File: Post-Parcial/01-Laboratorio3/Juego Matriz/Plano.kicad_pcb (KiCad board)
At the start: 2 copper layers, 122.7 x 77 mm, 33 parts, among them J1 Conn_01x12, J2 Conn_01x12, J3 Conn_01x19, J4 Conn_01x19, Q1 2N3904, Q2 2N3904, Q3 2N3904, Q4 2N3904, Q5 2N3904, Q6 2N3904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

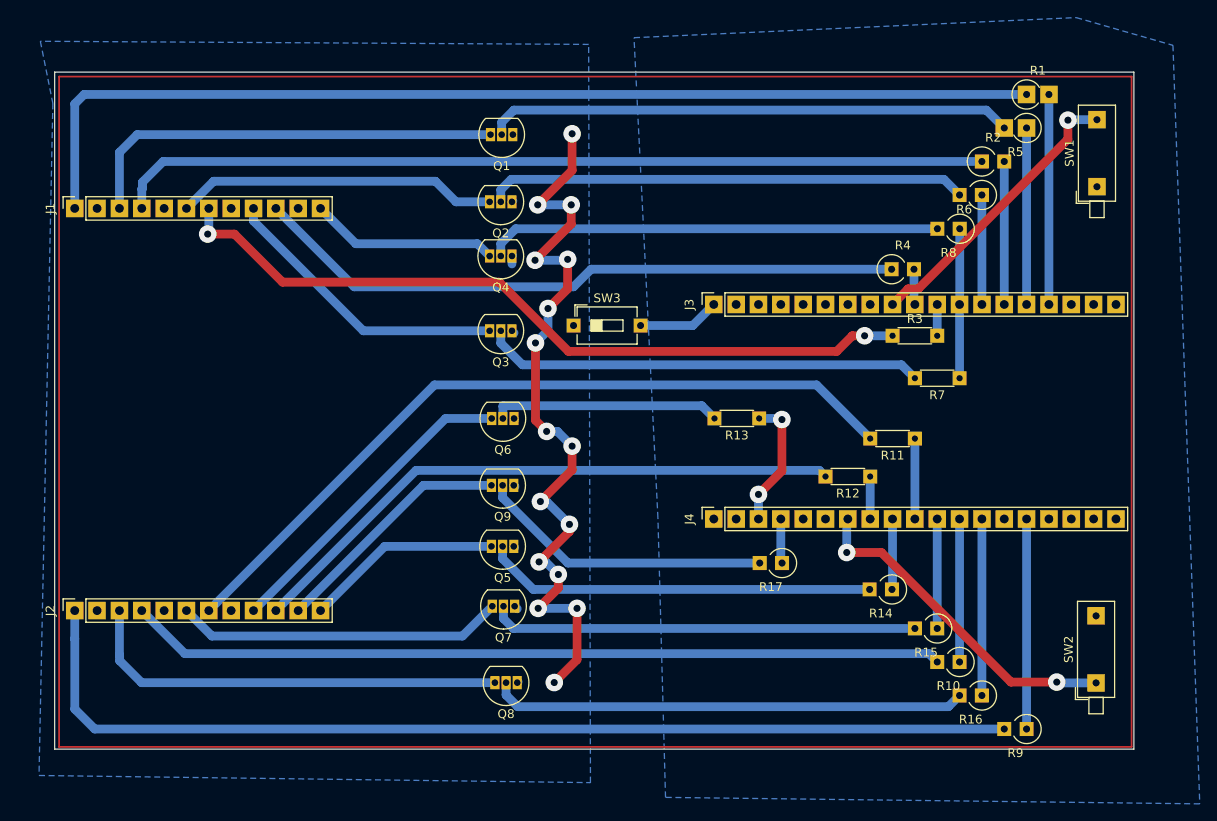
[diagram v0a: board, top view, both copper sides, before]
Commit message: Reorganización de PCB Juego Matriz
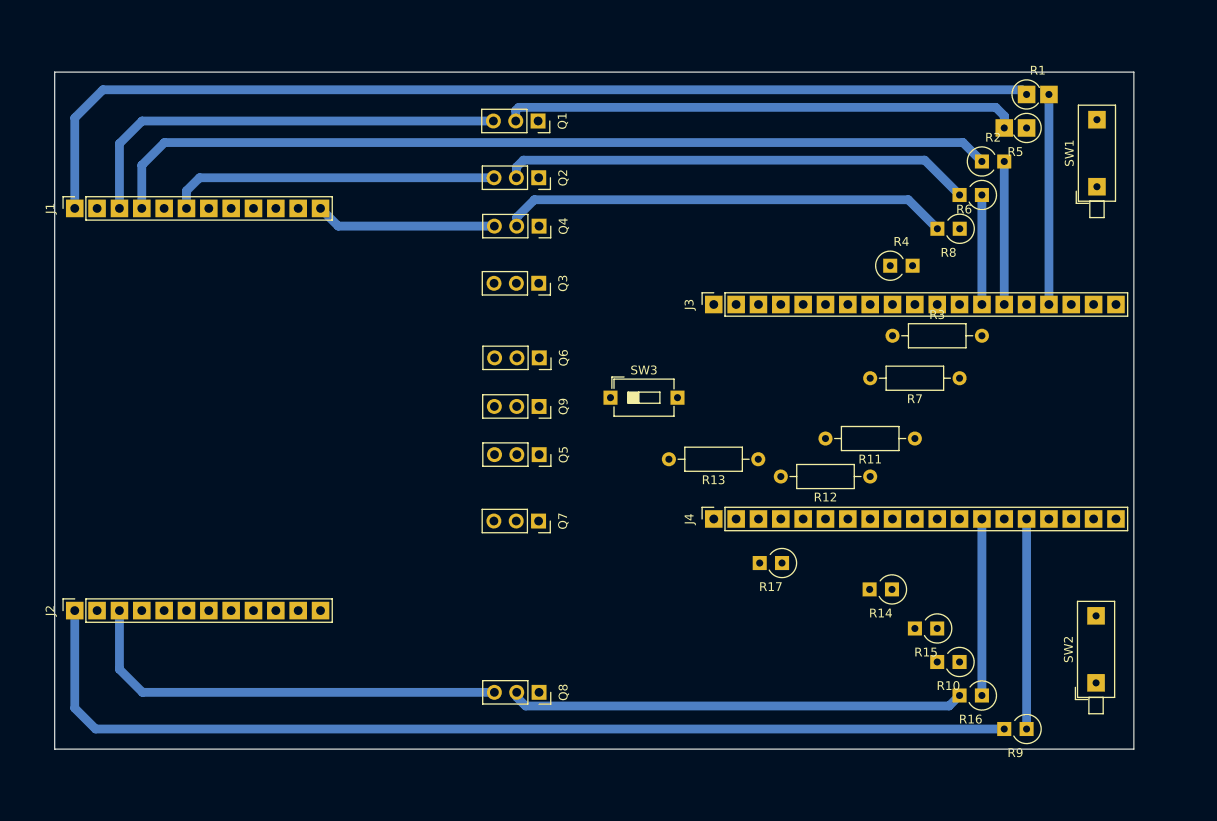
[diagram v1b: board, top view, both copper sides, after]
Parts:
- Q1, Q2, Q3, Q4, Q5, Q6, Q7, Q8, Q9: footprint Package_TO_SOT_THT:TO-92_Inline -> Connector_PinSocket_2.54mm:PinSocket_1x03_P2.54mm_Vertical
- R11, R12, R13, R3, R7: footprint Resistor_THT:R_Axial_DIN0204_L3.6mm_D1.6mm_P5.08mm_Horizontal -> Resistor_THT:R_Axial_DIN0207_L6.3mm_D2.5mm_P10.16mm_Horizontal
- moved Q5 10.8 mm to (151.1, 106.5), turned to -90 degrees
- moved Q7 10.1 mm to (151.0, 114.0), turned to -90 degrees
- moved Q9 9.42 mm to (151.1, 101.0), turned to -90 degrees
- moved SW3 9.21 mm to (159.2, 100.0)
- moved Q6 7.47 mm to (151.1, 95.5), turned to -90 degrees
- moved Q3 6.20 mm to (151.0, 87.0), turned to -90 degrees
- moved R13 4.64 mm to (176.0, 107.0)
- moved Q4 4.59 mm to (151.1, 80.5), turned to -90 degrees
- moved Q2 4.09 mm to (151.0, 75.0), turned to -90 degrees
- moved Q1 3.26 mm to (151.0, 68.5), turned to -90 degrees
- moved Q8 2.71 mm to (151.1, 133.5), turned to -90 degrees
- moved R4 0.43 mm to (191.0, 85.0)
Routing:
- net GND_BJT: track 92.9 -> 0.00 mm, vias 16 -> 0
- net GPIO14: track 92.8 -> 0.00 mm
- net GPIO26: track 88.3 -> 0.00 mm
- net GPIO17: track 87.1 -> 0.00 mm, vias 2 -> 0
- net GPIO5: track 74.5 -> 0.00 mm
- net GPIO33: track 69.4 -> 0.00 mm
- net Net-(Q3-B): track 50.1 -> 0.00 mm
- net Net-(Q7-B): track 48.6 -> 0.00 mm
- net Net-(Q5-B): track 44.6 -> 0.00 mm
- net GPIO32: track 38.3 -> 0.00 mm, vias 2 -> 0
- net Net-(J2-Pin_6): track 37.4 -> 0.00 mm
- net Net-(J2-Pin_9): track 36.1 -> 0.00 mm
- net Net-(Q9-B): track 33.7 -> 0.00 mm
- net Net-(J1-Pin_9): track 33.4 -> 0.00 mm
- net GPIO18: track 33.2 -> 0.00 mm, vias 1 -> 0
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- removed copper zone on B.Cu, net GND
- removed copper zone on B.Cu, net GND_BJT

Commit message: Avance nueva PCB juego matriz
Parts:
- R3, R7: footprint Resistor_THT:R_Axial_DIN0207_L6.3mm_D2.5mm_P10.16mm_Horizontal -> Resistor_THT:R_Axial_DIN0309_L9.0mm_D3.2mm_P2.54mm_Vertical
- R4: footprint Resistor_THT:R_Axial_DIN0309_L9.0mm_D3.2mm_P2.54mm_Vertical -> Resistor_THT:R_Axial_DIN0207_L6.3mm_D2.5mm_P10.16mm_Horizontal
- moved R4 28.8 mm to (163.3, 93.1)
- moved R11 28.7 mm to (165.8, 98.3), turned to 0 degrees
- moved R13 17.9 mm to (193.8, 104.9)
- moved R7 15.9 mm to (188.4, 85.8)
- moved Q5 13.6 mm to (151.2, 120.1)
- moved Q9 13.6 mm to (151.2, 114.6)
- moved Q7 12.5 mm to (151.1, 126.5)
- moved Q6 11.4 mm to (150.8, 106.8)
- moved R17 9.91 mm to (188.6, 117.9)
- moved SW3 9.85 mm to (151.1, 94.4)
- moved R3 8.65 mm to (193.8, 84.7)
- moved SW2 5.85 mm to (214.4, 126.6), turned to -90 degrees
- moved SW1 5.85 mm to (214.5, 70.2), turned to -90 degrees
- moved R12 2.58 mm to (186.2, 109.4)
- moved Q3 0.10 mm to (151.0, 87.1)
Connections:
- J1 pad 10: GPIO5 -> GPIO17
- J1 pad 7: GPIO17 -> GPIO23
- J2 pad 10: GPIO33 -> GPIO32
- J2 pad 7: GPIO26 -> GPIO22
- J3 pad 10: Net-(J3-Pin_10) -> GPIO5
- J3 pad 2: GPIO23 -> Net-(J3-Pin_2)
- J3 pad 3: GPIO22 -> Net-(J3-Pin_3)
- J4 pad 10: Net-(J4-Pin_10) -> GPIO26
- J4 pad 7: GPIO32 -> Net-(J4-Pin_7)
- J4 pad 8: Net-(J4-Pin_8) -> GPIO33
- R11 pad 1: Net-(J4-Pin_10) -> GPIO22
- R11 pad 2: GPIO26 -> Net-(J3-Pin_3)
- R12 pad 1: Net-(J4-Pin_8) -> Net-(J4-Pin_7)
- R12 pad 2: GPIO33 -> GPIO32
- R13 pad 1: GPI36 -> GPIO26
- R17 pad 1: GPI39 -> GPIO33
- R4 pad 1: GPIO5 -> GPIO23
- R4 pad 2: Net-(J3-Pin_10) -> Net-(J3-Pin_2)
- R7 pad 1: GPIO16 -> GPIO5
- R8 pad 1: unconnected-(R8-Pad1) -> GPIO16
- SW2 pad 1: GPIO32 -> GPI35
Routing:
- net GPIO14: track 0.00 -> 94.5 mm
- net GPIO17: track 0.00 -> 75.7 mm
- net GND_BJT: track 0.00 -> 74.4 mm, vias 0 -> 18
- net GPIO22: track 0.00 -> 64.2 mm
- net GPIO32: track 0.00 -> 62.0 mm
- net GPIO23: track 0.00 -> 56.3 mm
- net Net-(Q7-B): track 0.00 -> 47.3 mm
- net GPI35: track 0.00 -> 42.5 mm, vias 0 -> 1
- net Net-(Q5-B): track 0.00 -> 41.5 mm
- net Net-(Q9-B): track 0.00 -> 39.4 mm
- net Net-(Q3-B): track 0.00 -> 38.7 mm
- net Net-(J2-Pin_6): track 0.00 -> 37.4 mm
- net Net-(Q6-B): track 0.00 -> 36.6 mm
- net Net-(J2-Pin_9): track 0.00 -> 35.6 mm
- net GPIO18: track 0.00 -> 33.9 mm, vias 0 -> 1
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- added copper zone on B.Cu, net GND
- added copper zone on B.Cu, net GND_BJT

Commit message: PCB Juego Finalizada
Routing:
- net GPI35: track 42.5 -> 43.4 mm, vias 1 -> 2
- net GPIO18: track 33.9 -> 34.6 mm, vias 1 -> 2
- net Net-(J2-Pin_9): track 35.6 -> 36.2 mm

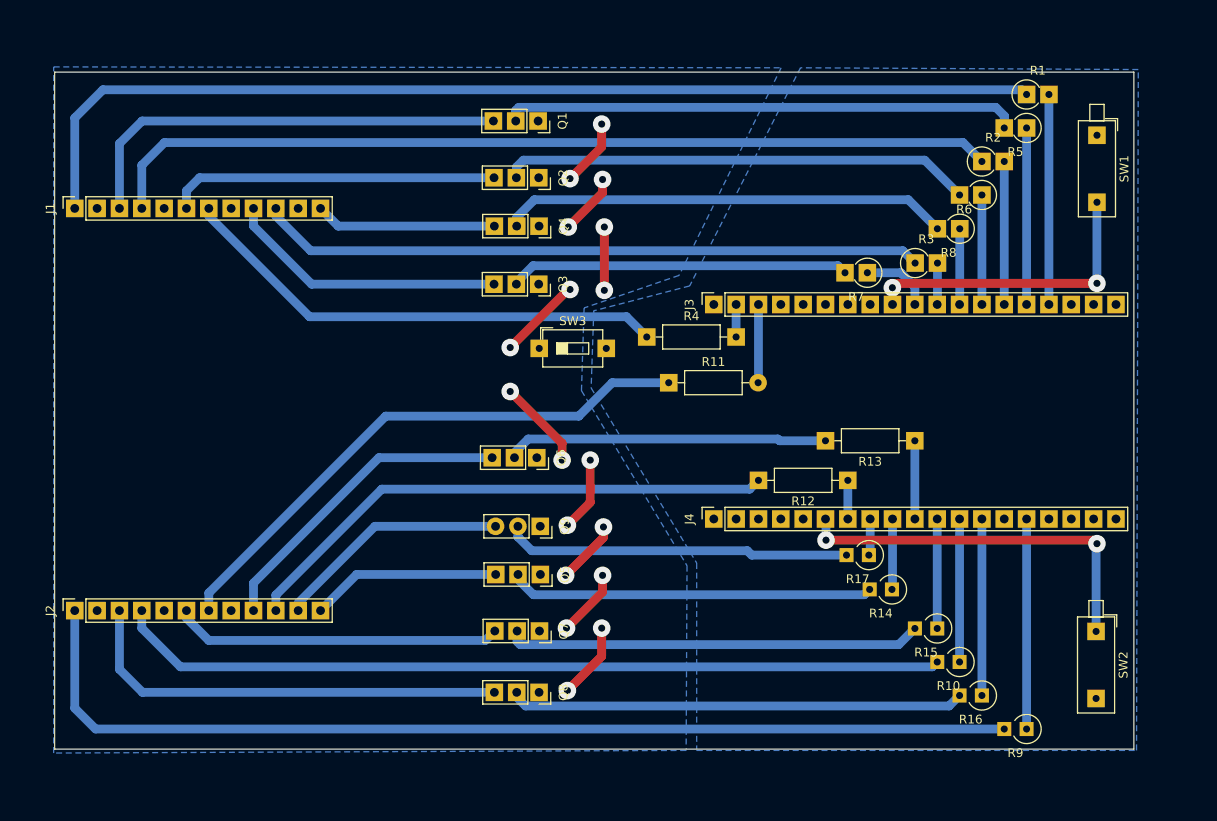
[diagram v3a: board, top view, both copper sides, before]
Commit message: Añadi Agujeros a la placa
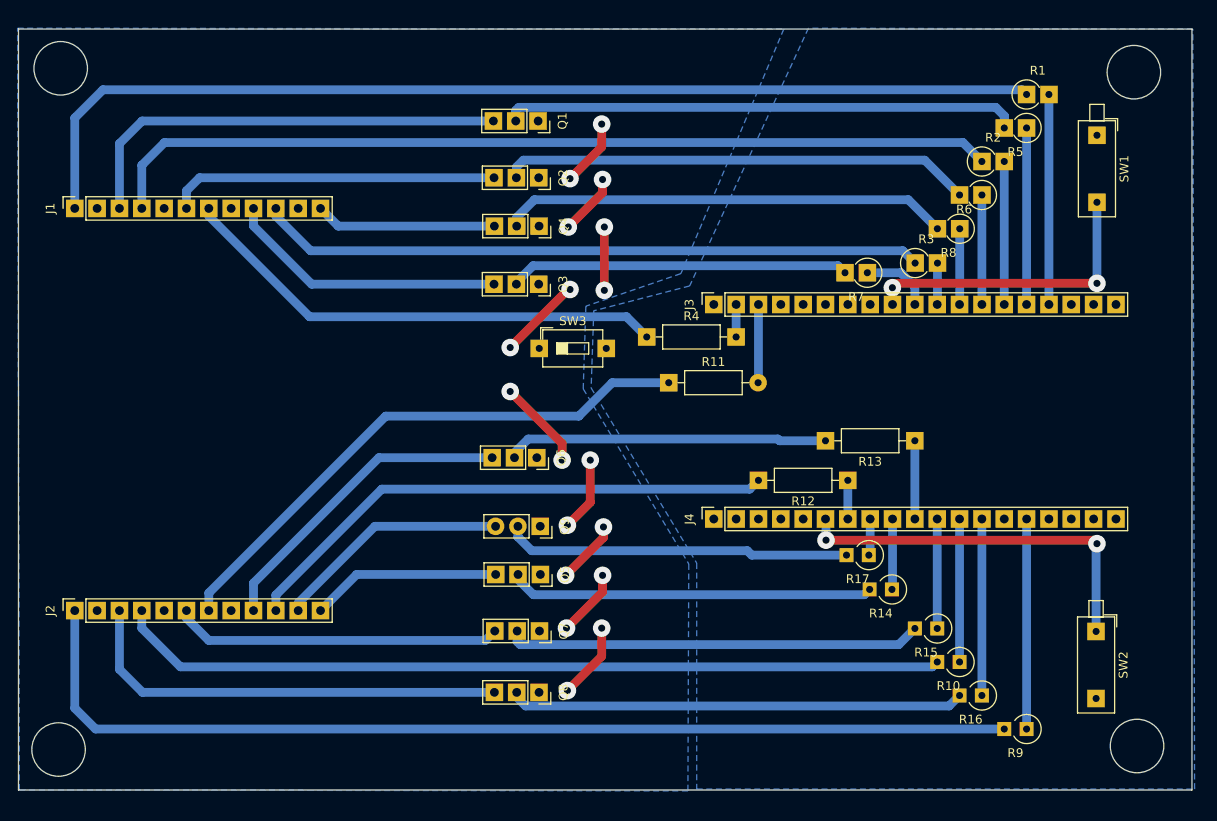
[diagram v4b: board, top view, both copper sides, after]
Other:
- board size 122.7 x 77 mm -> 133.4 x 86.5 mm
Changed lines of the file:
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@@
 		(layer "Dwgs.User")
 	)
+	(gr_circle
+		(center 218.7 63)
+		(end 220.9 60.9)
+		(stroke
+			(width 0.1)
+			(type default)
+		)
+		(fill none)
+		(layer "Edge.Cuts")
+	)
+	(gr_circle
+		(center 96.7 62.558619)
+		(end 98.9 60.458619)
+		(stroke
+			(width 0.1)
+			(type default)
+		)
+		(fill none)
+		(layer "Edge.Cuts")
+	)
 	(gr_rect
-		(start 96.012 62.992)
-		(end 218.694 139.954)
+		(start 91.9 58.1)
+		(end 225.3 144.6)
+		(stroke
+			(width 0.1)
+			(type default)
+		)
+		(fill none)
+		(layer "Edge.Cuts")
+	)
+	(gr_circle
+		(center 96.458619 140)
+		(end 98.658619 137.9)
+		(stroke
+			(width 0.1)
+			(type default)
+		)
+		(fill none)
+		(layer "Edge.Cuts")
+	)
+	(gr_circle
+		(center 219.058619 139.6)
+		(end 221.258619 137.5)
 		(stroke
 			(width 0.1)
@@
 		(layer "B.Cu")
 		(pts
-			(xy 96.792 125.978) (xy 96.792 76.708)
+			(xy 90.91 126) (xy 90.91 76.73)
 		)
 		(height -12.21)
 		(gr_text "49,2700 mm"
-			(at 82.782 101.343 90)
+			(at 76.9 101.365 90)
 			(layer "B.Cu")
 			(effects
@@
 		(polygon
 			(pts
-				(xy 157.3 90.1) (xy 157 98.9) (xy 169 118.8) (xy 169 140.1) (xy 219 140.1) (xy 219.2 62.7) (xy 180.8 62.5)
+				(xy 157.3 90.1) (xy 157 98.9) (xy 169 118.8) (xy 169 144.5) (xy 225.6 144.5) (xy 225.4 58.1) (xy 181.7 58)
 				(xy 168.2 87.3) (xy 157.4 90.1)
 			)
@@
 		(polygon
 			(pts
-				(xy 178.6 62.5) (xy 167 86.1) (xy 156.2 89.8) (xy 155.9 99.2) (xy 167.9 119.1) (xy 167.8 140.1)
-				(xy 95.9 140.4) (xy 95.9 62.4)
+				(xy 178.9 58.1) (xy 167.2 85.9) (xy 156.4 89.6) (xy 156.1 99) (xy 168.1 118.9) (xy 168 144.7) (xy 92 144.6)
+				(xy 91.8 58)
 			)
 		)
